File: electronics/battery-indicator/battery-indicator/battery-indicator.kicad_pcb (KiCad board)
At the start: 2 copper layers, 28 parts, among them J1 pwr-switch, J2 pwr, J3 battery, Q1 BC547, U1 LM358, U2 LM358

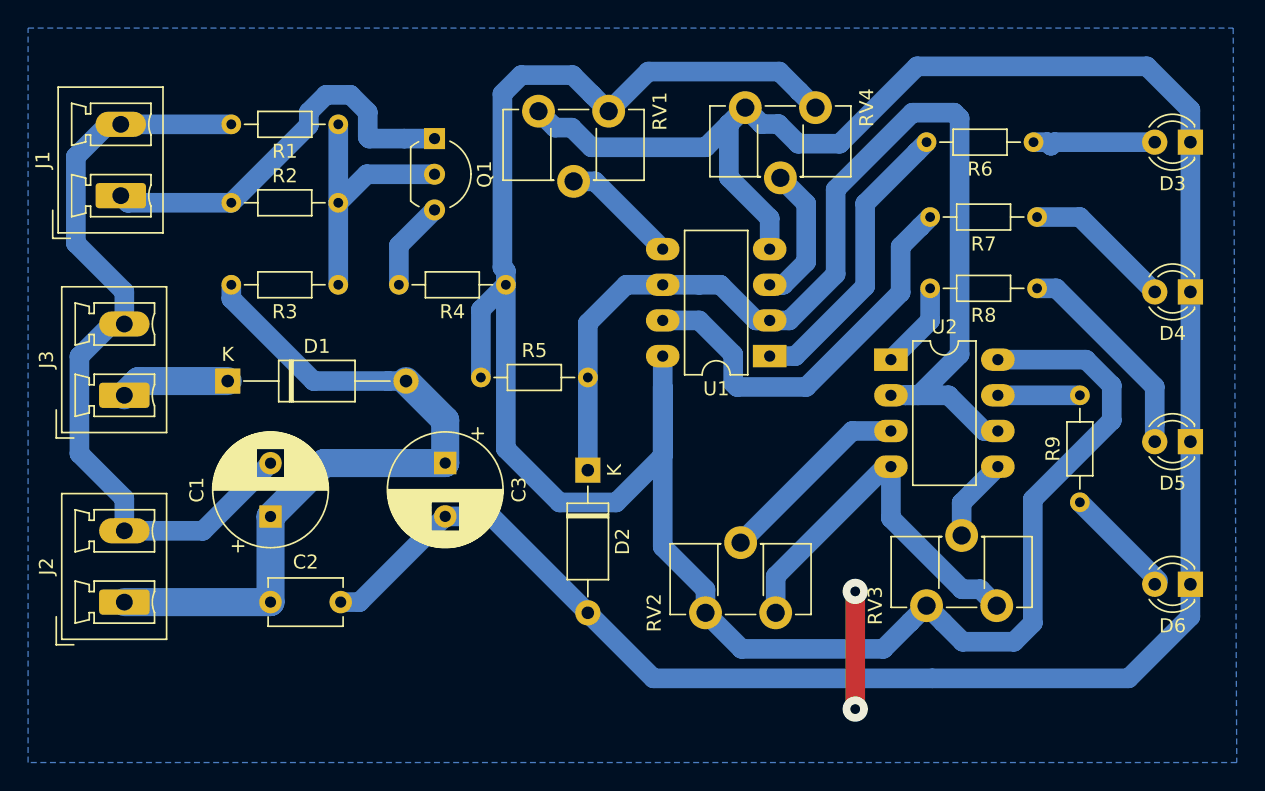
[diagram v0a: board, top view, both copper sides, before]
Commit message: Indicator but "or" is wrong
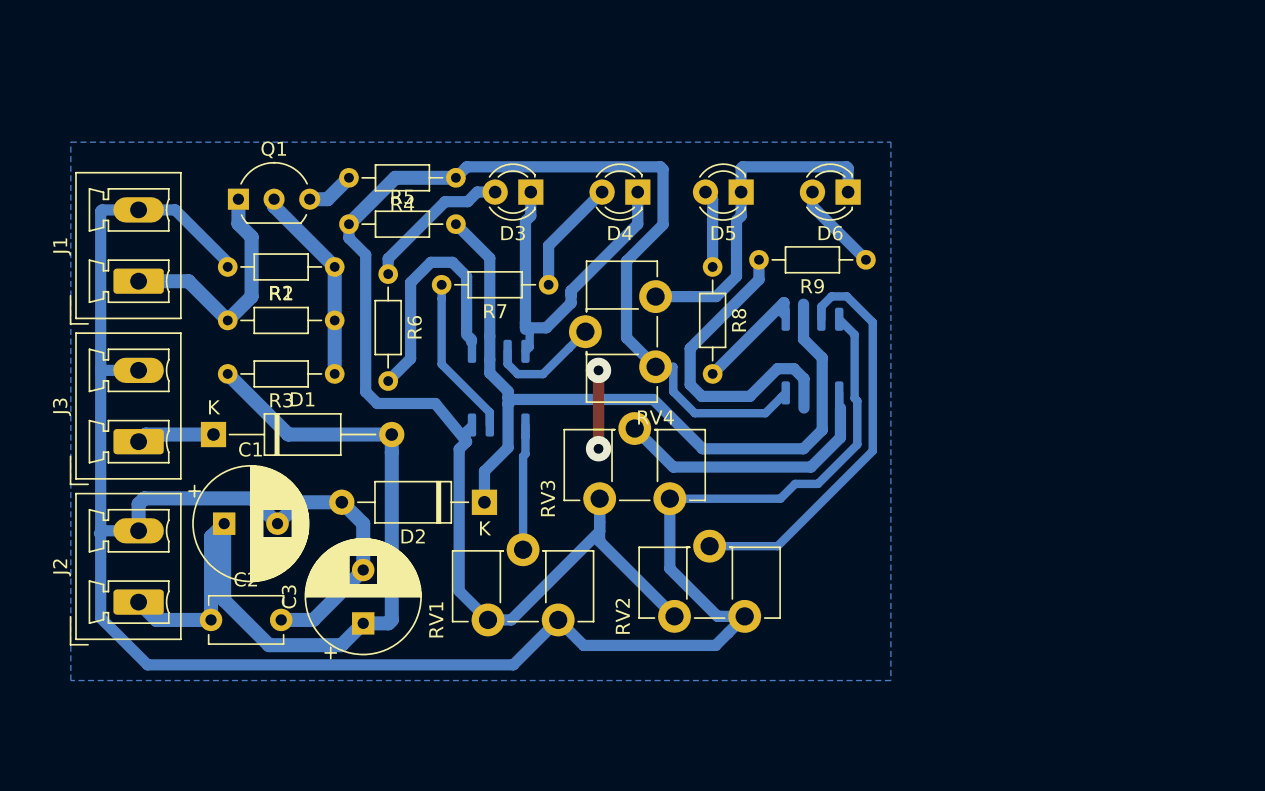
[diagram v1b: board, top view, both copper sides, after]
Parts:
- U1, U2: footprint Package_DIP:DIP-8_W7.62mm_LongPads -> Package_SO:SOP-8_3.9x4.9mm_P1.27mm; moved to B.Cu
- moved D3 47.1 mm to (84.6, 60.7)
- moved R6 46.9 mm to (74.4, 66.5), turned to 270 degrees
- moved D4 40.0 mm to (92.2, 60.7)
- moved RV1 37.2 mm to (81.5, 91.2), turned to 90 degrees
- moved D6 37.1 mm to (107.2, 60.7)
- moved D5 36.6 mm to (99.6, 60.7)
- moved R7 35.1 mm to (85.9, 67.3)
- moved RV3 24.5 mm to (89.5, 82.5)
- moved R8 23.2 mm to (97.5, 66.0), turned to 270 degrees
- moved R9 23.0 mm to (108.5, 65.5), turned to 180 degrees
- moved RV4 21.7 mm to (93.5, 73.2), turned to 180 degrees
- moved U1 19.4 mm to (82.3, 74.7), turned to 270 degrees
- moved Q1 14.6 mm to (63.8, 61.2), turned to 0 degrees
- moved R5 14.4 mm to (71.6, 63.0)
- moved C3 12.8 mm to (72.6, 91.4), turned to 90 degrees
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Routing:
- net GND: track 261.1 -> 218.2 mm
- net Net-(R4-Pad1): track 152.9 -> 112.3 mm
- net Net-(D2-Pad1): track 79.6 -> 56.1 mm
- net Net-(R7-Pad2): track 29.1 -> 11.4 mm
- net Net-(R9-Pad2): track 5.84 -> 22.6 mm
- net Net-(RV2-Pad2): track 14.0 -> 29.2 mm
- net Net-(RV3-Pad2): track 5.97 -> 19.9 mm
- net Net-(J1-Pad1): track 28.6 -> 17.2 mm
- net Net-(D5-Pad2): track 15.2 -> 5.54 mm
- net Net-(C1-Pad1): track 53.4 -> 59.1 mm
- net Net-(Q1-Pad2): track 19.1 -> 14.2 mm
- net Net-(R6-Pad2): track 20.9 -> 17.1 mm
- net Net-(Q1-Pad3): track 6.39 -> 3.43 mm
- net Net-(D4-Pad2): track 10.6 -> 8.18 mm
- net Net-(D1-Pad1): track 7.79 -> 5.54 mm
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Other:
- net class Default: clearance 0.7 -> 0.5; trace_width 1.4 -> 0.6
- rule trace_clearance: 0.7 -> 0.5
